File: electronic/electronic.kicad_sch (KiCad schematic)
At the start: 62 parts, among them J1 M_PWM, J10 BMP01, J11 MPU6050_01, J12 NEO_06_01, J13 CONN, J14 OLED, J15 HCSR01, J16 HCSR02, J17 HCSR03, J18 HCSR04, J2 BAT_AX, J20 25.5-24 ESP32, J9 DHT01, U10 DEVKIT_V1_ESP32-WROOM-32, U11 RT9193-33GB, U12 CAT24C256, U13 SSD1306, U15 HC-SR04, U16 HC-SR04, U17 HC-SR04, U18 HC-SR04, U5 BMP280, U6 DHT22, U7 AP2112K-1.2, U8 NEO-6M-GPS, U9 MPU-6050

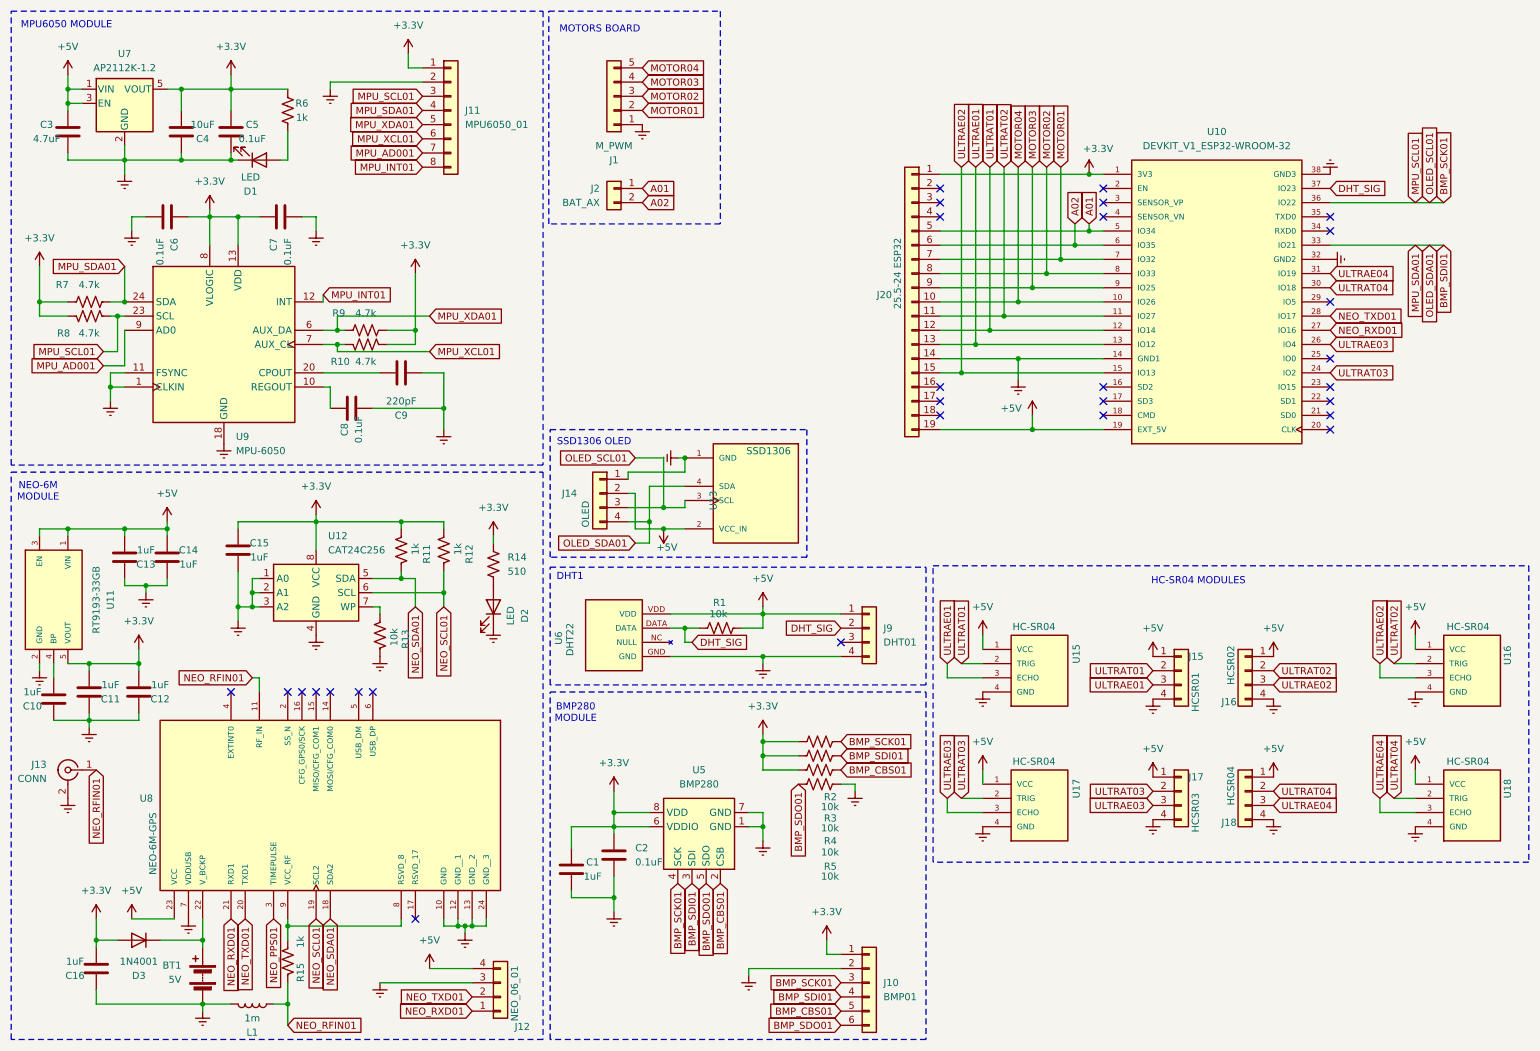
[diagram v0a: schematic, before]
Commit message: feat (electronic): Unify electronic and power PCBs into one
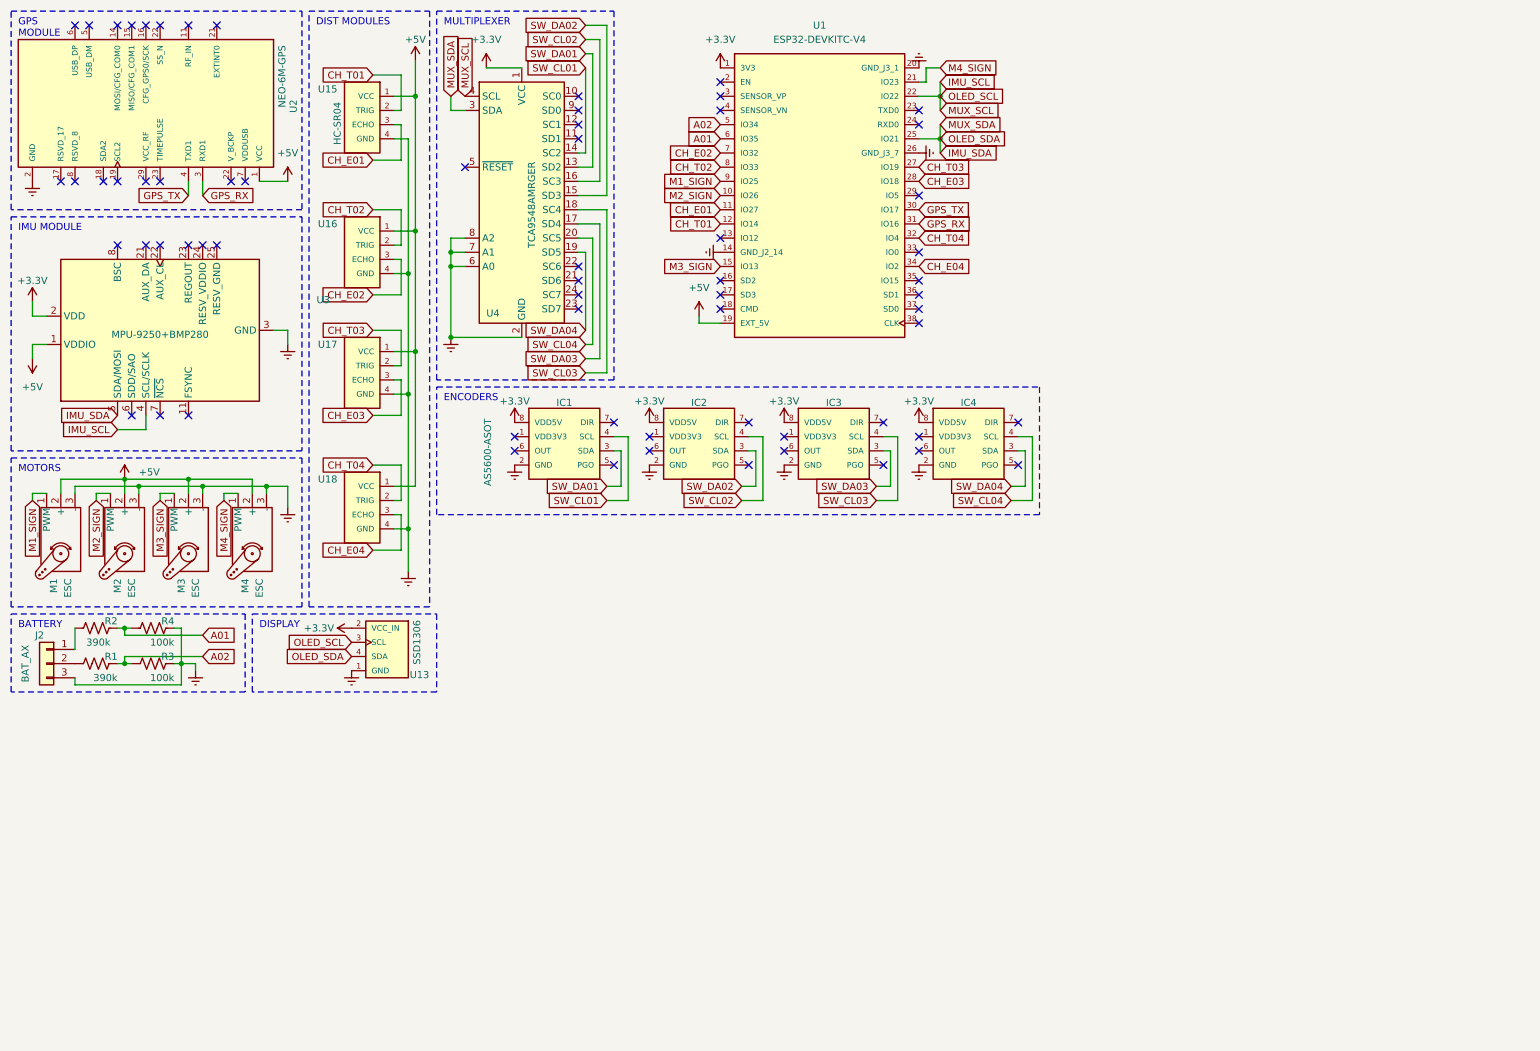
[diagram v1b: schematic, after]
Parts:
- removed BT1: 5V, symbol Device:Battery
- removed C1, C10, C11, C12, C13, C14, C15, C16: 1uF, symbol Device:C
- removed C2, C5, C6, C7, C8: 0.1uF, symbol Device:C
- removed C3: 4.7uF, symbol Device:C
- removed C4: 10uF, symbol Device:C
- removed C9: 220pF, symbol Device:C
- removed D1, D2: LED, LED_SMD:LED_0402_1005Metric, symbol Device:LED
- removed D3: 1N4001, Diode_THT:D_DO-41_SOD81_P10.16mm_Horizontal, symbol Diode:1N4001
- removed J1: M_PWM, Connector_JST:JST_XH_B5B-XH-A_1x05_P2.50mm_Vertical, symbol Connector_Generic:Conn_01x05
- removed J10: BMP01, Connector_PinHeader_2.54mm:PinHeader_1x06_P2.54mm_Vertical, symbol Connector_Generic:Conn_01x06
- removed J11: MPU6050_01, Connector_PinHeader_2.54mm:PinHeader_1x08_P2.54mm_Vertical, symbol Connector_Generic:Conn_01x08
- removed J12: NEO_06_01, Connector_PinHeader_2.54mm:PinHeader_1x04_P2.54mm_Vertical, symbol Connector_Generic:Conn_01x04
- removed J13: CONN, symbol Connector:Conn_Coaxial
- removed J14: OLED, Connector_PinHeader_2.54mm:PinHeader_1x04_P2.54mm_Vertical, symbol Connector_Generic:Conn_01x04
- removed J15: HCSR01, Connector_PinHeader_2.54mm:PinHeader_1x04_P2.54mm_Vertical, symbol Connector_Generic:Conn_01x04
- removed J16: HCSR02, Connector_PinHeader_2.54mm:PinHeader_1x04_P2.54mm_Vertical, symbol Connector_Generic:Conn_01x04
- removed J17: HCSR03, Connector_PinHeader_2.54mm:PinHeader_1x04_P2.54mm_Vertical, symbol Connector_Generic:Conn_01x04
- removed J18: HCSR04, Connector_PinHeader_2.54mm:PinHeader_1x04_P2.54mm_Vertical, symbol Connector_Generic:Conn_01x04
- removed J20: 25.5-24 ESP32, Connector_PinSocket_2.54mm:PinSocket_1x19_P2.54mm_Vertical, symbol Connector_Generic:Conn_01x19
- removed J9: DHT01, custom:DHT22, symbol Connector_Generic:Conn_01x04
- removed L1: 1m, symbol Device:L
- removed R10, R7, R8, R9: 4.7k, symbol Device:R_US
- removed R11, R12, R15, R6: 1k, symbol Device:R_US
- removed R13, R5: 10k, symbol Device:R_US
- removed R14: 510, symbol Device:R_US
- removed U10: DEVKIT_V1_ESP32-WROOM-32, custom:MODULE_DEVKIT_V1_ESP32-WROOM-32, symbol DEVKIT_V1_ESP32-WROOM-32:DEVKIT_V1_ESP32-WROOM-32
- removed U11: RT9193-33GB, RT9193-33GB:SOT23-5_TEXAS_INSTRUMETNS, symbol RT9193-33GB:RT9193-33GB
- removed U12: CAT24C256, symbol Memory_EEPROM:CAT24C256
- removed U5: BMP280, Package_LGA:Bosch_LGA-8_2x2.5mm_P0.65mm_ClockwisePinNumbering, symbol Sensor_Pressure:BMP280
- removed U6: DHT22, custom:DHT22, symbol DHT22:DHT22
- removed U7: AP2112K-1.2, Package_TO_SOT_SMD:SOT-23-5, symbol Regulator_Linear:AP2112K-1.2
- removed U8: NEO-6M-GPS, NEO-6M-GPS:XCVR_NEO-6M-GPS, symbol NEO-6M-GPS:NEO-6M-GPS
- removed U9: MPU-6050, Sensor_Motion:InvenSense_QFN-24_4x4mm_P0.5mm, symbol Sensor_Motion:MPU-6050
- added IC1, IC2, IC3, IC4: AS5600-ASOT, AS5600-ASOT:SOIC127P600X175-8N, symbol AS5600-ASOT:AS5600-ASOT
- added M1, M2, M3, M4: ESC, Connector_PinSocket_2.54mm:PinSocket_1x03_P2.54mm_Horizontal, symbol Motor:Motor_Servo
- added U1: ESP32-DEVKITC-V4, local:MODULE_ESP32-DEVKITC-V4, symbol ESP32-DEVKITC-32E:ESP32-DEVKITC-V4
- added U2: NEO-6M-GPS, Connector_PinHeader_2.54mm:PinHeader_1x04_P2.54mm_Vertical, symbol NEO-6M-GPS:NEO-6M-GPS
- added U3: MPU-9250+BMP280, local:MPU9250, symbol mpu9250:MPU-9250
- added U4: TCA9548AMRGER, local:TCA9548A, symbol tca9548a:TCA9548AMRGER
- J2: footprint Connector_JST:JST_XH_B2B-XH-A_1x02_P2.50mm_Vertical -> Connector_JST:JST_XH_B3B-XH-A_1x03_P2.50mm_Vertical; symbol Connector_Generic:Conn_01x02 -> Connector_Generic:Conn_01x03
- R1: value 10k -> 390k; footprint Resistor_THT:R_Axial_DIN0207_L6.3mm_D2.5mm_P10.16mm_Horizontal -> Resistor_SMD:R_0805_2012Metric
- R2: value 10k -> 390k; footprint (none) -> Resistor_SMD:R_0805_2012Metric; now in the parts list
- R3, R4: value 10k -> 100k; footprint (none) -> Resistor_SMD:R_0805_2012Metric; now in the parts list
- U13: footprint custom:MODULE_DM-OLED096-636 -> local:MODULE_DM-OLED096-636; symbol custom:DM-OLED096-636 -> DM-OLED096-636:DM-OLED096-636
- U15, U16, U17, U18: Availability Not in stock -> In Stock
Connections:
- net BMP_CBS01 is gone; now on net Earth: R4.2
- net DHT_SIG is gone; now on net A02: R1.2
- net +3.3V: now also U13.2 (VCC_IN), IC1.8 (VDD5V), IC2.8 (VDD5V), IC3.8 (VDD5V), IC4.8 (VDD5V), U1.1 (3V3), U3.2 (VDD), U4.1 (VCC); no longer R2.1, R3.1, R4.1
- net +5V: now also M1.2 (+), M2.2 (+), M3.2 (+), M4.2 (+), U1.19 (EXT_5V), U2.1 (VCC), U3.1 (VDDIO); no longer R1.1, U13.2 (VCC_IN)
- net A01: now also R2.2, R4.1, U1.6 (IO35); no longer J2.1 (Pin_1)
- net A02: now also R3.1, U1.5 (IO34); no longer J2.2 (Pin_2)
- net Earth: now also J2.3 (Pin_3), R3.2, IC1.2 (GND), IC2.2 (GND), IC3.2 (GND), IC4.2 (GND), M1.3 (-), M2.3 (-), M3.3 (-), M4.3 (-), U1.14 (GND_J2_14), U1.20 (GND_J3_1), U1.26 (GND_J3_7), U2.12 (GND), U2.13 (GND), U2.2 (GND), U2.24 (GND), U3.3 (GND), U4.2 (GND), U4.6 (A0), U4.7 (A1), U4.8 (A2)
- net BMP_SCK01 renamed IMU_SCL
- net IMU_SCL: now also U1.22 (IO22), U3.4 (SCL/SCLK), U4.4 (SCL); no longer R2.2
- net BMP_SDI01 renamed IMU_SDA
- net IMU_SDA: now also U1.25 (IO21), U3.5 (SDA/MOSI), U4.3 (SDA); no longer R3.2
- net ULTRAE01 renamed CH_E01
- net CH_E01: now also U1.11 (IO27)
- net ULTRAE02 renamed CH_E02
- net CH_E02: now also U1.7 (IO32)
- net ULTRAE03 renamed CH_E03
- net CH_E03: now also U1.28 (IO18)
- net ULTRAE04 renamed CH_E04
- net CH_E04: now also U1.34 (IO2)
- net ULTRAT01 renamed CH_T01
- net CH_T01: now also U1.12 (IO14)
- net ULTRAT02 renamed CH_T02
- net CH_T02: now also U1.8 (IO33)
- net ULTRAT03 renamed CH_T03
- net CH_T03: now also U1.27 (IO19)
- net ULTRAT04 renamed CH_T04
- net CH_T04: now also U1.32 (IO4)
- new net: J2.1 (Pin_1), R2.1
- new net: J2.2 (Pin_2), R1.1
- new net GPS_RX: U1.31 (IO16), U2.3 (RXD1)
- new net GPS_TX: U1.30 (IO17), U2.4 (TXD1)
- new net M1_SIGN: M1.1 (PWM), U1.9 (IO25)
- new net M2_SIGN: M2.1 (PWM), U1.10 (IO26)
- new net M3_SIGN: M3.1 (PWM), U1.15 (IO13)
- new net M4_SIGN: M4.1 (PWM), U1.21 (IO23)
- new net SW_CL01: IC1.4 (SCL), U4.14 (SC2)
- new net SW_CL02: IC2.4 (SCL), U4.16 (SC3)
- new net SW_CL03: IC3.4 (SCL), U4.18 (SC4)
- new net SW_CL04: IC4.4 (SCL), U4.20 (SC5)
- new net SW_DA01: IC1.3 (SDA), U4.13 (SD2)
- new net SW_DA02: IC2.3 (SDA), U4.15 (SD3)
- new net SW_DA03: IC3.3 (SDA), U4.17 (SD4)
- new net SW_DA04: IC4.3 (SDA), U4.19 (SD5)
- no-connect marks 29 -> 65
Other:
- note added: "BATTERY"
- note added: "DISPLAY"
- note added: "DIST MODULES"
- note added: "ENCODERS"
- note added: "GPS MODULE"
- note added: "IMU MODULE"
- note added: "MOTORS"
- note added: "MULTIPLEXER"
- note removed: "BMP280 MODULE"
- note removed: "DHT1"
- note removed: "HC-SR04 MODULES"
- note removed: "MOTORS BOARD"
- note removed: "MPU6050 MODULE"
- note removed: "NEO-6M MODULE"
- note removed: "SSD1306 OLED"
- moved on the sheet: U13, U15, U16, U17, U18
